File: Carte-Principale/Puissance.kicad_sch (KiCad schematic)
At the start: 0 parts

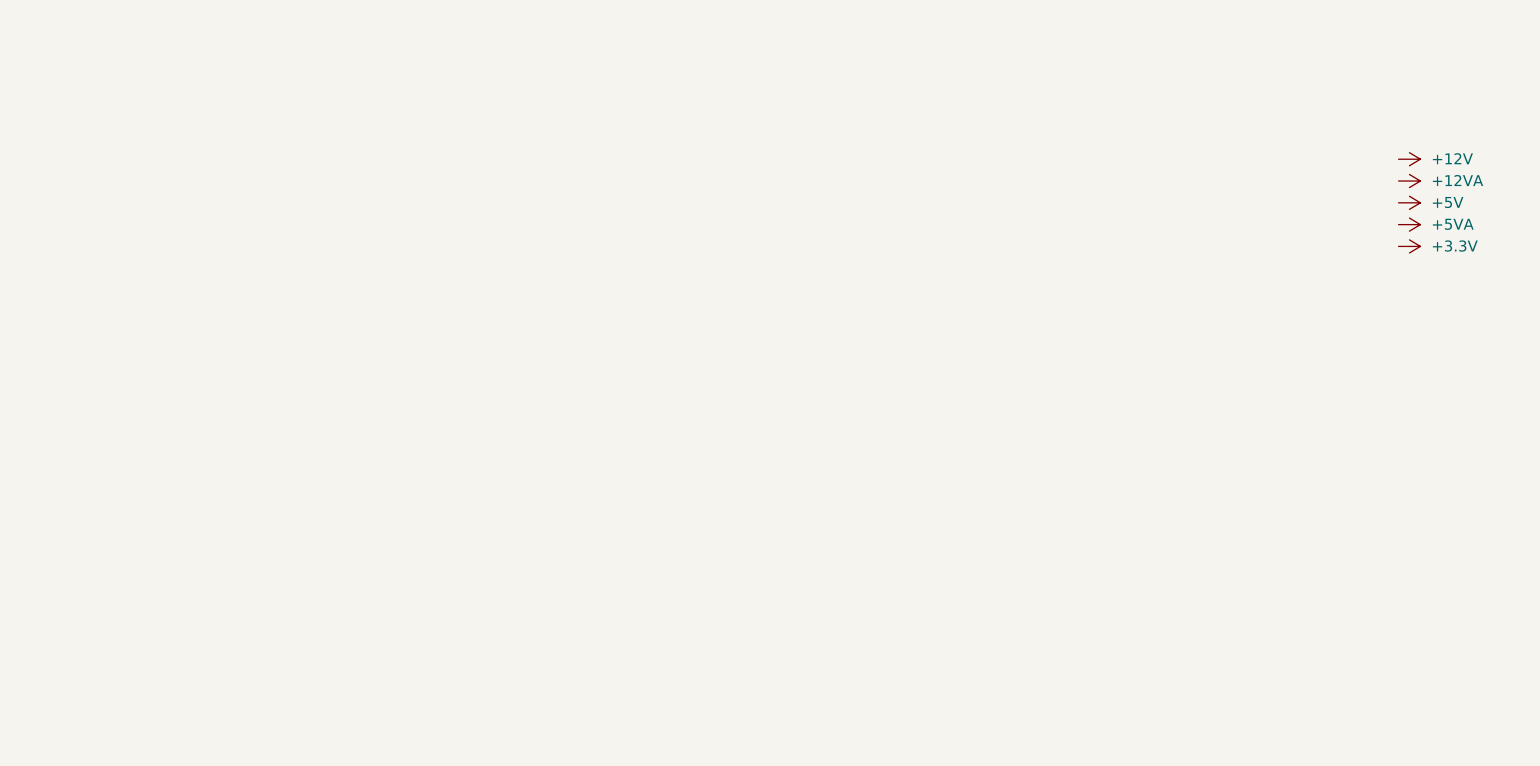
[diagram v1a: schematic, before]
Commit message: Rajout écran
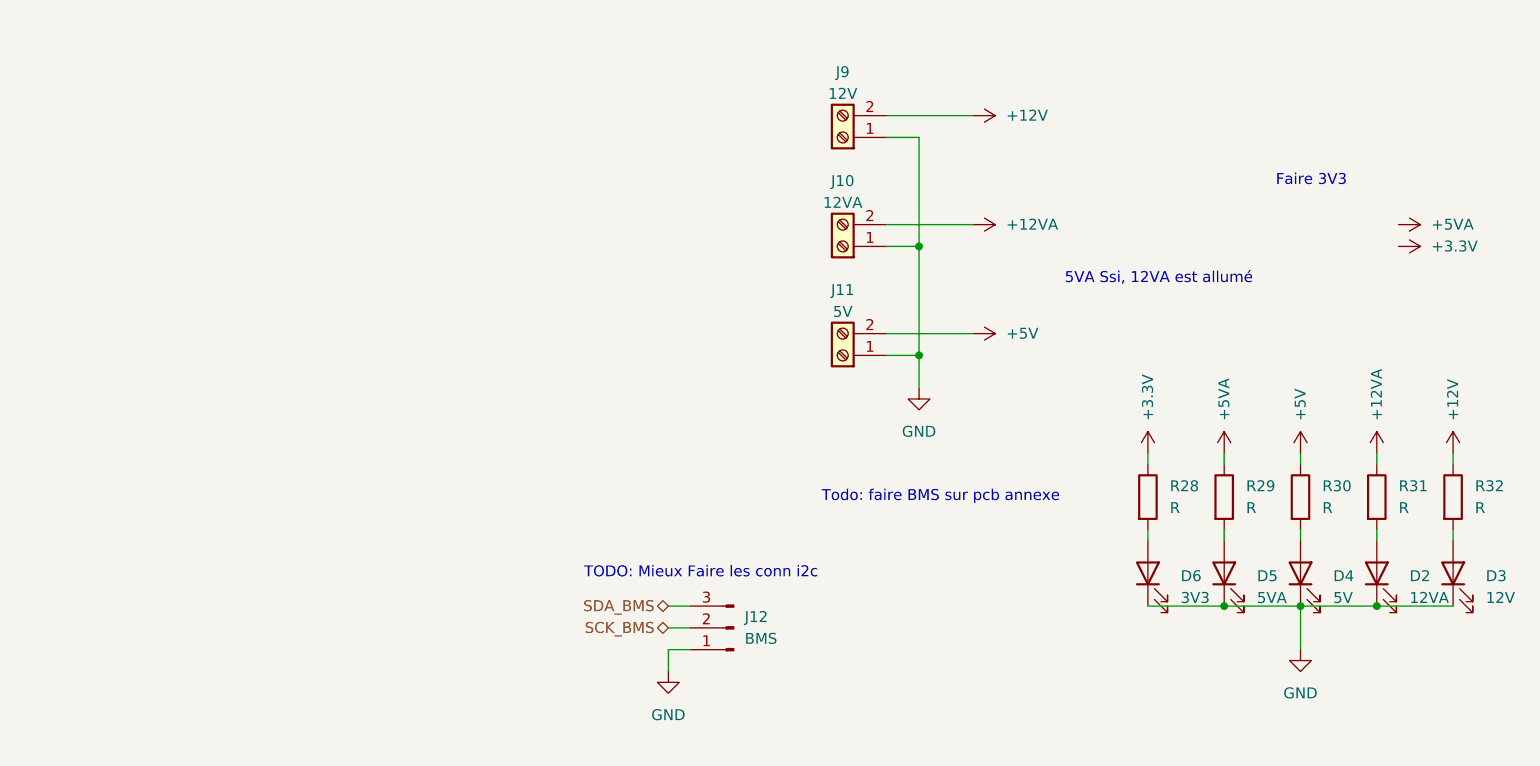
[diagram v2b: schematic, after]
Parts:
- added D2: 12VA, symbol Device:LED
- added D3: 12V, symbol Device:LED
- added D4: 5V, symbol Device:LED
- added D5: 5VA, symbol Device:LED
- added D6: 3V3, symbol Device:LED
- added J10: 12VA, symbol Connector:Screw_Terminal_01x02
- added J11: 5V, symbol Connector:Screw_Terminal_01x02
- added J12: BMS, symbol Connector:Conn_01x03_Pin
- added J9: 12V, symbol Connector:Screw_Terminal_01x02
- added R28, R29, R30, R31, R32: R, symbol Device:R
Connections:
- net +12V: now also J9.2 (Pin_2), R32.1
- net +12VA: now also J10.2 (Pin_2), R31.1
- net +3.3V: now also R28.1
- net +5V: now also J11.2 (Pin_2), R30.1
- net +5VA: now also R29.1
- new net: D5.2 (A), R29.2
- new net: D4.2 (A), R30.2
- new net: D6.2 (A), R28.2
- new net: D3.2 (A), R32.2
- new net: D2.2 (A), R31.2
- new net GND: D2.1 (K), D3.1 (K), D4.1 (K), D5.1 (K), D6.1 (K), J10.1 (Pin_1), J11.1 (Pin_1), J12.1 (Pin_1), J9.1 (Pin_1)
- new net SCK_BMS: J12.2 (Pin_2)
- new net SDA_BMS: J12.3 (Pin_3)
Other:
- note added: "5VA Ssi, 12VA est allumé"
- note added: "Faire 3V3"
- note added: "TODO: Mieux Faire les conn i2c"
- note added: "Todo: faire BMS sur pcb annexe"

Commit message: wiring
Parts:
- removed J12: BMS, symbol Connector:Conn_01x03_Pin
- added Q1: NMOS, symbol Simulation_SPICE:NMOS
- added R1: 10K, Resistor_SMD:R_1206_3216Metric_Pad1.30x1.75mm_HandSolder, symbol Device:R
- D1: renamed from D6; footprint (none) -> LED_SMD:LED_2010_5025Metric_Pad1.52x2.65mm_HandSolder
- D2: renamed from D5; footprint (none) -> LED_SMD:LED_2010_5025Metric_Pad1.52x2.65mm_HandSolder
- D3: renamed from D4; footprint (none) -> LED_SMD:LED_2010_5025Metric_Pad1.52x2.65mm_HandSolder
- D4: renamed from D2; footprint (none) -> LED_SMD:LED_2010_5025Metric_Pad1.52x2.65mm_HandSolder
- D5: renamed from D3; footprint (none) -> LED_SMD:LED_2010_5025Metric_Pad1.52x2.65mm_HandSolder
- J1: renamed from J9; footprint (none) -> TerminalBlock:TerminalBlock_bornier-2_P5.08mm
- J2: renamed from J10; footprint (none) -> TerminalBlock:TerminalBlock_bornier-2_P5.08mm
- J3: renamed from J11; footprint (none) -> TerminalBlock:TerminalBlock_bornier-2_P5.08mm
- R2: renamed from R28; footprint (none) -> Resistor_SMD:R_1206_3216Metric_Pad1.30x1.75mm_HandSolder
- R3: renamed from R29; footprint (none) -> Resistor_SMD:R_1206_3216Metric_Pad1.30x1.75mm_HandSolder
- R4: renamed from R30; footprint (none) -> Resistor_SMD:R_1206_3216Metric_Pad1.30x1.75mm_HandSolder
- R5: renamed from R31; footprint (none) -> Resistor_SMD:R_1206_3216Metric_Pad1.30x1.75mm_HandSolder
- R6: renamed from R32; footprint (none) -> Resistor_SMD:R_1206_3216Metric_Pad1.30x1.75mm_HandSolder
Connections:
- net +12VA: now also Q1.2 (G), R1.1
- net +5V: now also Q1.1 (D)
- net +5VA: now also Q1.3 (S)
- net GND: now also R1.2
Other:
- note added: "12VA asservi par BAU"
- note added: "TODO: Reverse voltage protection"
- note added: "trouver mosfet"
- note removed: "5VA Ssi, 12VA est allumé"
- note removed: "Faire 3V3"
- note removed: "TODO: Mieux Faire les conn i2c"
- moved on the sheet: J1, J2, J3

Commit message: Schéma vérifié
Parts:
- removed J1: 12V, TerminalBlock:TerminalBlock_bornier-2_P5.08mm, symbol Connector:Screw_Terminal_01x02
- removed J2: 12VA, TerminalBlock:TerminalBlock_bornier-2_P5.08mm, symbol Connector:Screw_Terminal_01x02
- removed J3: 5V, TerminalBlock:TerminalBlock_bornier-2_P5.08mm, symbol Connector:Screw_Terminal_01x02
- removed Q1: NMOS, symbol Simulation_SPICE:NMOS
- added F2: 2A, Fuse:Fuse_2010_5025Metric_Pad1.52x2.65mm_HandSolder, symbol Device:Polyfuse
- added F3, F4: 5A, Fuse:Fuse_2010_5025Metric_Pad1.52x2.65mm_HandSolder, symbol Device:Polyfuse
- added J10: 5V, Connector_AMASS:AMASS_XT30U-M_1x02_P5.0mm_Vertical, symbol Connector:Conn_01x02_Socket
- added J8: 12V, Connector_AMASS:AMASS_XT60-M_1x02_P7.20mm_Vertical, symbol Connector:Conn_01x02_Socket
- added J9: 12VA, Connector_AMASS:AMASS_XT60-M_1x02_P7.20mm_Vertical, symbol Connector:Conn_01x02_Socket
- added Q1: IRF630, Package_TO_SOT_THT:TO-220-3_Vertical, symbol Transistor_FET:NDT3055L
- added TP1: GND, Connector_Pin:Pin_D1.0mm_L10.0mm, symbol Connector:TestPoint
- added TP2: 3V3, Connector_Pin:Pin_D1.0mm_L10.0mm, symbol Connector:TestPoint
- added TP3: 5VA, Connector_Pin:Pin_D1.0mm_L10.0mm, symbol Connector:TestPoint
- added TP4: 5V, Connector_Pin:Pin_D1.0mm_L10.0mm, symbol Connector:TestPoint
- added TP5: 12VA, Connector_Pin:Pin_D1.0mm_L10.0mm, symbol Connector:TestPoint
- added TP6: 12V, Connector_Pin:Pin_D1.0mm_L10.0mm, symbol Connector:TestPoint
- R1, R2, R3, R4, R5, R6: footprint Resistor_SMD:R_1206_3216Metric_Pad1.30x1.75mm_HandSolder -> Resistor_SMD:R_1210_3225Metric_Pad1.30x2.65mm_HandSolder
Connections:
- net +12V: now also F2.2, TP6.1
- net +12VA: now also F3.2, Q1.1 (G), TP5.1
- net +3.3V: now also TP2.1
- net +5V: now also F4.2, Q1.2 (D), TP4.1
- net +5VA: now also Q1.3 (S), TP3.1
- net GND: now also J10.1 (Pin_1), J8.1 (Pin_1), J9.1 (Pin_1), TP1.1
- new net: F3.1, J9.2 (Pin_2)
- new net: F4.1, J10.2 (Pin_2)
- new net: F2.1, J8.2 (Pin_2)
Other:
- note removed: "TODO: Reverse voltage protection"
- note removed: "trouver mosfet"
- company: (none) -> CRINSA
- title: (none) -> Carte Principale
- moved on the sheet: D1, D2, D3, D4, D5, R1, R2, R3, R4, R5, R6

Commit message: Avancée PCB
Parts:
- removed D5: 12V, LED_SMD:LED_2010_5025Metric_Pad1.52x2.65mm_HandSolder, symbol Device:LED
- removed F2: 2A, Fuse:Fuse_2010_5025Metric_Pad1.52x2.65mm_HandSolder, symbol Device:Polyfuse
- removed J8: 12V, Connector_AMASS:AMASS_XT60-M_1x02_P7.20mm_Vertical, symbol Connector:Conn_01x02_Socket
- removed R6: R, Resistor_SMD:R_1210_3225Metric_Pad1.30x2.65mm_HandSolder, symbol Device:R
- removed TP6: 12V, Connector_Pin:Pin_D1.0mm_L10.0mm, symbol Connector:TestPoint
- renumbered F3 to F2, F4 to F3, J9 to J6, J10 to J7

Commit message: avancée
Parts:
- renumbered D3 to D4, D2 to D5, D1 to D6, D4 to D7, F3 to F1, J6 to J2, J7 to J3, R2 to R1, R5 to R3, R3 to R4, R1 to R7, R4 to R8, TP2 to TP1, TP4 to TP2, TP1 to TP3, TP3 to TP4
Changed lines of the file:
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@@
 		(dnp no)
 		(fields_autoplaced yes)
-		(property "Reference" "D2"
+		(property "Reference" "D5"
 			(at 152.4 85.4074 90)
 			(effects
@@
 			(project "Carte-Principale"
 				(path "/88b0dd29-ac24-4c5d-804c-fc642ecf6263/7eed38b4-f789-4722-81cb-a4e4542631b4"
-					(reference "D2")
+					(reference "D5")
 					(unit 1)
 				)
@@
 		(dnp no)
 		(fields_autoplaced yes)
-		(property "Reference" "R4"
+		(property "Reference" "R8"
 			(at 160.02 74.9299 0)
 			(effects
@@
 			(project "Carte-Principale"
 				(path "/88b0dd29-ac24-4c5d-804c-fc642ecf6263/7eed38b4-f789-4722-81cb-a4e4542631b4"
-					(reference "R4")
+					(reference "R8")
 					(unit 1)
 				)
@@
 		(dnp no)
 		(fields_autoplaced yes)
-		(property "Reference" "TP4"
+		(property "Reference" "TP2"
 			(at 154.178 63.5 90)
 			(effects
@@
 			(project "Carte-Principale"
 				(path "/88b0dd29-ac24-4c5d-804c-fc642ecf6263/7eed38b4-f789-4722-81cb-a4e4542631b4"
-					(reference "TP4")
+					(reference "TP2")
 					(unit 1)
 				)
@@
 		(dnp no)
 		(fields_autoplaced yes)
-		(property "Reference" "R2"
+		(property "Reference" "R1"
 			(at 142.24 74.9299 0)
 			(effects
@@
 			(project "Carte-Principale"
 				(path "/88b0dd29-ac24-4c5d-804c-fc642ecf6263/7eed38b4-f789-4722-81cb-a4e4542631b4"
-					(reference "R2")
+					(reference "R1")
 					(unit 1)
 				)
@@
 		(dnp no)
 		(fields_autoplaced yes)
-		(property "Reference" "D1"
+		(property "Reference" "D6"
 			(at 143.51 85.4074 90)
 			(effects
@@
 			(project "Carte-Principale"
 				(path "/88b0dd29-ac24-4c5d-804c-fc642ecf6263/7eed38b4-f789-4722-81cb-a4e4542631b4"
-					(reference "D1")
+					(reference "D6")
 					(unit 1)
 				)
@@
 		(dnp no)
 		(fields_autoplaced yes)
-		(property "Reference" "F3"
+		(property "Reference" "F1"
 			(at 66.04 49.53 90)
 			(effects
@@
 			(project "Carte-Principale"
 				(path "/88b0dd29-ac24-4c5d-804c-fc642ecf6263/7eed38b4-f789-4722-81cb-a4e4542631b4"
-					(reference "F3")
+					(reference "F1")
 					(unit 1)
 				)
@@
 		(dnp no)
 		(fields_autoplaced yes)
-		(property "Reference" "J6"
+		(property "Reference" "J2"
 			(at 48.895 38.1 0)
 			(effects
@@
 			(project "Carte-Principale"
 				(path "/88b0dd29-ac24-4c5d-804c-fc642ecf6263/7eed38b4-f789-4722-81cb-a4e4542631b4"
-					(reference "J6")
+					(reference "J2")
 					(unit 1)
 				)
@@
 		(dnp no)
 		(fields_autoplaced yes)
-		(property "Reference" "R3"
+		(property "Reference" "R4"
 			(at 151.13 74.9299 0)
 			(effects
@@
 			(project "Carte-Principale"
 				(path "/88b0dd29-ac24-4c5d-804c-fc642ecf6263/7eed38b4-f789-4722-81cb-a4e4542631b4"
-					(reference "R3")
+					(reference "R4")
 					(unit 1)
 				)
@@
 		(dnp no)
 		(fields_autoplaced yes)
-		(property "Reference" "D3"
+		(property "Reference" "D4"
 			(at 161.29 85.4074 90)
 			(effects
@@
 			(project "Carte-Principale"
 				(path "/88b0dd29-ac24-4c5d-804c-fc642ecf6263/7eed38b4-f789-4722-81cb-a4e4542631b4"
-					(reference "D3")
+					(reference "D4")
 					(unit 1)
 				)
@@
 		(dnp no)
 		(fields_autoplaced yes)
-		(property "Reference" "R5"
+		(property "Reference" "R3"
 			(at 168.91 74.9299 0)
 			(effects
@@
 			(project "Carte-Principale"
 				(path "/88b0dd29-ac24-4c5d-804c-fc642ecf6263/7eed38b4-f789-4722-81cb-a4e4542631b4"
-					(reference "R5")
+					(reference "R3")
 					(unit 1)
 				)
@@
 		(on_board yes)
 		(dnp no)
-		(property "Reference" "R1"
+		(property "Reference" "R7"
 			(at 139.7 43.18 90)
 			(effects
@@
 			(project "Carte-Principale"
 				(path "/88b0dd29-ac24-4c5d-804c-fc642ecf6263/7eed38b4-f789-4722-81cb-a4e4542631b4"
-					(reference "R1")
+					(reference "R7")
 					(unit 1)
 				)
@@
 		(dnp no)
 		(fields_autoplaced yes)
-		(property "Reference" "TP3"
+		(property "Reference" "TP4"
 			(at 145.288 63.5 90)
 			(effects
@@
 			(project "Carte-Principale"
 				(path "/88b0dd29-ac24-4c5d-804c-fc642ecf6263/7eed38b4-f789-4722-81cb-a4e4542631b4"
-					(reference "TP3")
+					(reference "TP4")
 					(unit 1)
 				)
@@
 		(dnp no)
 		(fields_autoplaced yes)
-		(property "Reference" "TP2"
+		(property "Reference" "TP1"
 			(at 136.398 63.5 90)
 			(effects
@@
 			(project "Carte-Principale"
 				(path "/88b0dd29-ac24-4c5d-804c-fc642ecf6263/7eed38b4-f789-4722-81cb-a4e4542631b4"
-					(reference "TP2")
+					(reference "TP1")
 					(unit 1)
 				)
@@
 		(on_board yes)
 		(dnp no)
-		(property "Reference" "TP1"
+		(property "Reference" "TP3"
 			(at 112.268 62.23 90)
 			(effects
@@
 			(project "Carte-Principale"
 				(path "/88b0dd29-ac24-4c5d-804c-fc642ecf6263/7eed38b4-f789-4722-81cb-a4e4542631b4"
-					(reference "TP1")
+					(reference "TP3")
 					(unit 1)
 				)
@@
 		(dnp no)
 		(fields_autoplaced yes)
-		(property "Reference" "D4"
+		(property "Reference" "D7"
 			(at 170.18 85.4074 90)
 			(effects
@@
 			(project "Carte-Principale"
 				(path "/88b0dd29-ac24-4c5d-804c-fc642ecf6263/7eed38b4-f789-4722-81cb-a4e4542631b4"
-					(reference "D4")
+					(reference "D7")
 					(unit 1)
 				)
@@
 		(dnp no)
 		(fields_autoplaced yes)
-		(property "Reference" "J7"
+		(property "Reference" "J3"
 			(at 48.895 50.8 0)
 			(effects
@@
 			(project "Carte-Principale"
 				(path "/88b0dd29-ac24-4c5d-804c-fc642ecf6263/7eed38b4-f789-4722-81cb-a4e4542631b4"
-					(reference "J7")
-					(unit 1)
-				)
+					(reference "J3")
+					(unit 1)
+				)

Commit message: Final pcb modification
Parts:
- renumbered D5 to D4, D4 to D5, F2 to F1, F1 to F2, J2 to J3, J3 to J4, R8 to R3, R3 to R4, R7 to R6, R4 to R8, TP3 to TP2, TP2 to TP3
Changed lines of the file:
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@@
 		(dnp no)
 		(fields_autoplaced yes)
-		(property "Reference" "D5"
+		(property "Reference" "D4"
 			(at 152.4 85.4074 90)
 			(effects
@@
 			(project "Carte-Principale"
 				(path "/88b0dd29-ac24-4c5d-804c-fc642ecf6263/7eed38b4-f789-4722-81cb-a4e4542631b4"
-					(reference "D5")
+					(reference "D4")
 					(unit 1)
 				)
@@
 		(dnp no)
 		(fields_autoplaced yes)
-		(property "Reference" "R8"
+		(property "Reference" "R3"
 			(at 160.02 74.9299 0)
 			(effects
@@
 			(project "Carte-Principale"
 				(path "/88b0dd29-ac24-4c5d-804c-fc642ecf6263/7eed38b4-f789-4722-81cb-a4e4542631b4"
-					(reference "R8")
+					(reference "R3")
 					(unit 1)
 				)
@@
 		(dnp no)
 		(fields_autoplaced yes)
-		(property "Reference" "TP2"
+		(property "Reference" "TP3"
 			(at 154.178 63.5 90)
 			(effects
@@
 			(project "Carte-Principale"
 				(path "/88b0dd29-ac24-4c5d-804c-fc642ecf6263/7eed38b4-f789-4722-81cb-a4e4542631b4"
-					(reference "TP2")
+					(reference "TP3")
 					(unit 1)
 				)
@@
 		(dnp no)
 		(fields_autoplaced yes)
-		(property "Reference" "F2"
+		(property "Reference" "F1"
 			(at 66.04 36.83 90)
 			(effects
@@
 			(project "Carte-Principale"
 				(path "/88b0dd29-ac24-4c5d-804c-fc642ecf6263/7eed38b4-f789-4722-81cb-a4e4542631b4"
-					(reference "F2")
+					(reference "F1")
 					(unit 1)
 				)
@@
 		(dnp no)
 		(fields_autoplaced yes)
-		(property "Reference" "F1"
+		(property "Reference" "F2"
 			(at 66.04 49.53 90)
 			(effects
@@
 			(project "Carte-Principale"
 				(path "/88b0dd29-ac24-4c5d-804c-fc642ecf6263/7eed38b4-f789-4722-81cb-a4e4542631b4"
-					(reference "F1")
+					(reference "F2")
 					(unit 1)
 				)
@@
 		(dnp no)
 		(fields_autoplaced yes)
-		(property "Reference" "J2"
+		(property "Reference" "J3"
 			(at 48.895 38.1 0)
 			(effects
@@
 			(project "Carte-Principale"
 				(path "/88b0dd29-ac24-4c5d-804c-fc642ecf6263/7eed38b4-f789-4722-81cb-a4e4542631b4"
-					(reference "J2")
+					(reference "J3")
 					(unit 1)
 				)
@@
 		(dnp no)
 		(fields_autoplaced yes)
-		(property "Reference" "R4"
+		(property "Reference" "R8"
 			(at 151.13 74.9299 0)
 			(effects
@@
 			(project "Carte-Principale"
 				(path "/88b0dd29-ac24-4c5d-804c-fc642ecf6263/7eed38b4-f789-4722-81cb-a4e4542631b4"
-					(reference "R4")
+					(reference "R8")
 					(unit 1)
 				)
@@
 		(dnp no)
 		(fields_autoplaced yes)
-		(property "Reference" "D4"
+		(property "Reference" "D5"
 			(at 161.29 85.4074 90)
 			(effects
@@
 			(project "Carte-Principale"
 				(path "/88b0dd29-ac24-4c5d-804c-fc642ecf6263/7eed38b4-f789-4722-81cb-a4e4542631b4"
-					(reference "D4")
+					(reference "D5")
 					(unit 1)
 				)
@@
 		(dnp no)
 		(fields_autoplaced yes)
-		(property "Reference" "R3"
+		(property "Reference" "R4"
 			(at 168.91 74.9299 0)
 			(effects
@@
 			(project "Carte-Principale"
 				(path "/88b0dd29-ac24-4c5d-804c-fc642ecf6263/7eed38b4-f789-4722-81cb-a4e4542631b4"
-					(reference "R3")
+					(reference "R4")
 					(unit 1)
 				)
@@
 		(on_board yes)
 		(dnp no)
-		(property "Reference" "R7"
+		(property "Reference" "R6"
 			(at 139.7 43.18 90)
 			(effects
@@
 			(project "Carte-Principale"
 				(path "/88b0dd29-ac24-4c5d-804c-fc642ecf6263/7eed38b4-f789-4722-81cb-a4e4542631b4"
-					(reference "R7")
+					(reference "R6")
 					(unit 1)
 				)
@@
 		(on_board yes)
 		(dnp no)
-		(property "Reference" "TP3"
+		(property "Reference" "TP2"
 			(at 112.268 62.23 90)
 			(effects
@@
 			(project "Carte-Principale"
 				(path "/88b0dd29-ac24-4c5d-804c-fc642ecf6263/7eed38b4-f789-4722-81cb-a4e4542631b4"
-					(reference "TP3")
+					(reference "TP2")
 					(unit 1)
 				)
@@
 		(dnp no)
 		(fields_autoplaced yes)
-		(property "Reference" "J3"
+		(property "Reference" "J4"
 			(at 48.895 50.8 0)
 			(effects
@@
 			(project "Carte-Principale"
 				(path "/88b0dd29-ac24-4c5d-804c-fc642ecf6263/7eed38b4-f789-4722-81cb-a4e4542631b4"
-					(reference "J3")
-					(unit 1)
-				)
+					(reference "J4")
+					(unit 1)
+				)

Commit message: Cartes élec à refaire et TODO
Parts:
- removed D4: 5VA, LED_SMD:LED_2010_5025Metric_Pad1.52x2.65mm_HandSolder, symbol Device:LED
- removed Q1: IRF630, Package_TO_SOT_THT:TO-220-3_Vertical, symbol Transistor_FET:NDT3055L
- removed R6: 10K, Resistor_SMD:R_1210_3225Metric_Pad1.30x2.65mm_HandSolder, symbol Device:R
- removed R8: R, Resistor_SMD:R_1210_3225Metric_Pad1.30x2.65mm_HandSolder, symbol Device:R
- removed TP4: 5VA, Connector_Pin:Pin_D1.0mm_L10.0mm, symbol Connector:TestPoint
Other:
- moved on the sheet: D6, R1, TP1
